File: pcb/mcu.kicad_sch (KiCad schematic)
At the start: 1 part, among them U1 STM32L432KCUx

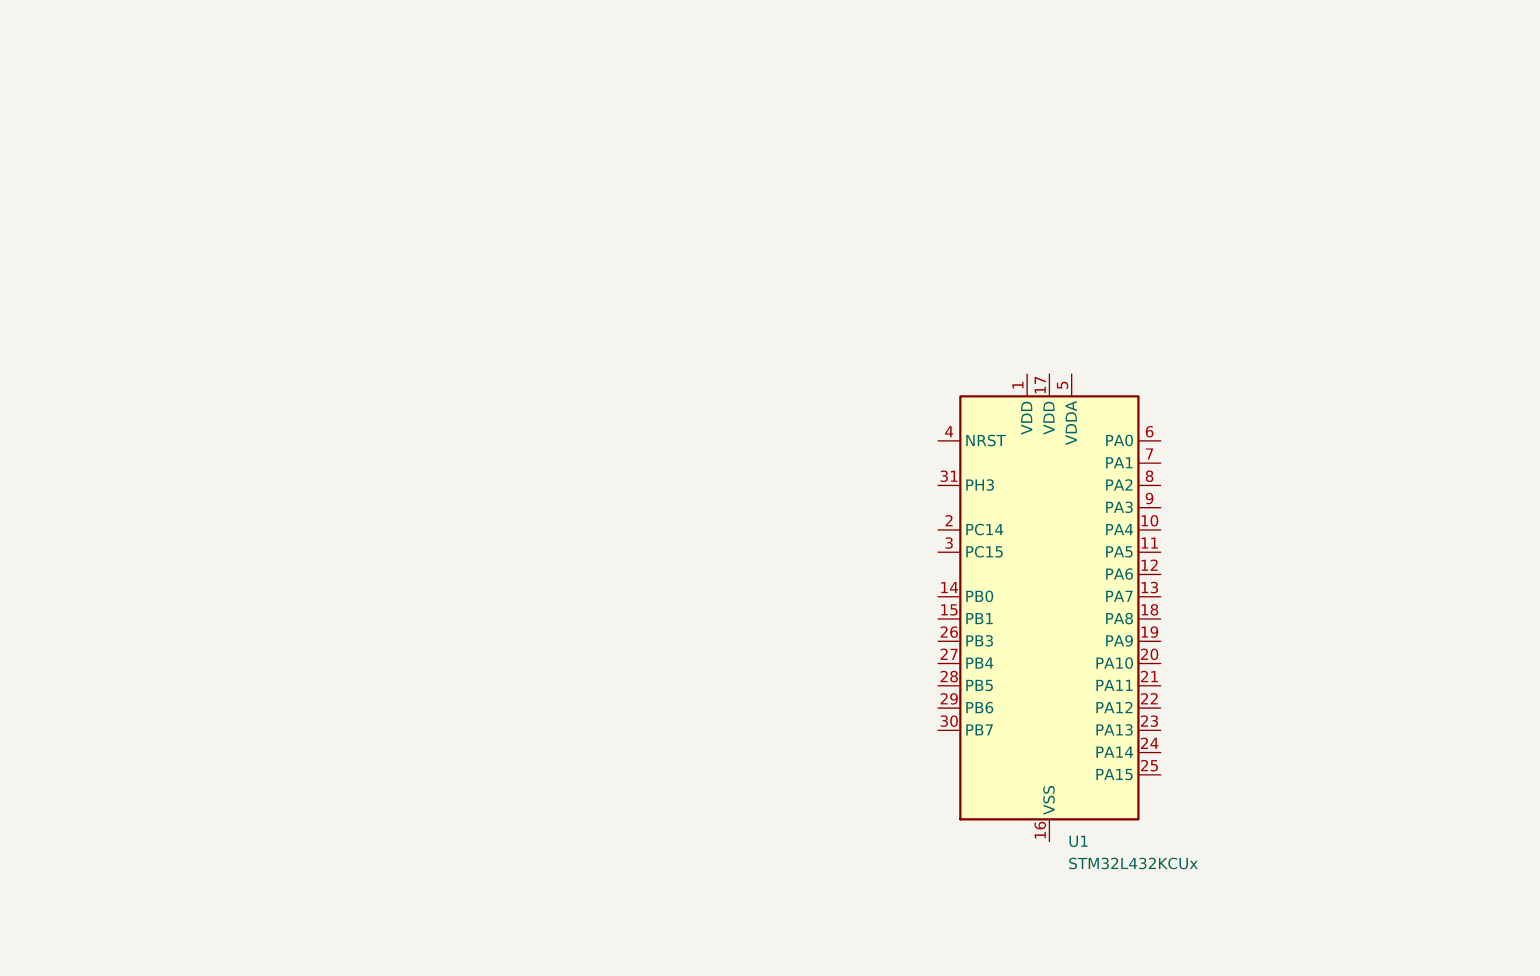
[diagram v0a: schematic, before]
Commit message: Sch almost done, maybe add current sense
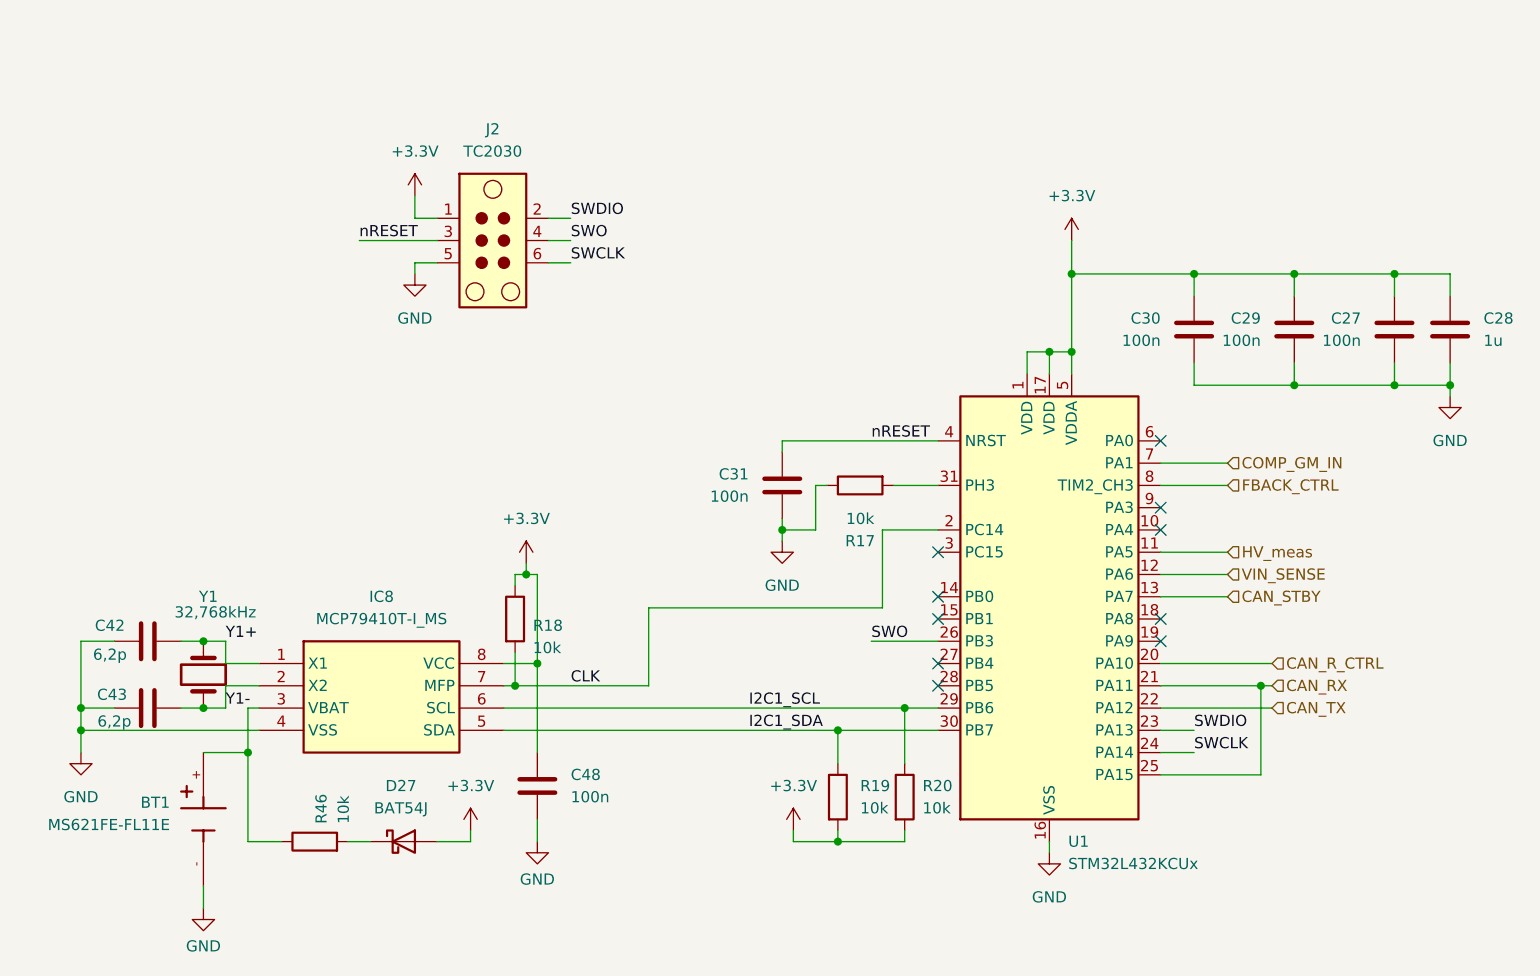
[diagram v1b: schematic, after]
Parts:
- added BT1: MS621FE-FL11E, Battery:BAT_MS621FE-FL11E, symbol MS621FE-FL11E:MS621FE-FL11E
- added C27, C29, C30, C31: 100n, Capacitor_SMD:C_0603_1608Metric, symbol Device:C
- added C28: 1u, Capacitor_SMD:C_0603_1608Metric, symbol Device:C
- added C42, C43: 6,2p, Capacitor_SMD:C_0402_1005Metric_Pad0.74x0.62mm_HandSolder, symbol Device:C
- added C48: 100n, Capacitor_SMD:C_0603_1608Metric_Pad1.08x0.95mm_HandSolder, symbol Device:C
- added D27: BAT54J, Diode_SMD:D_SOD-323F, symbol Diode:BAT54J
- added IC8: MCP79410T-I_MS, SOP65P490X110-8N, symbol SamacSys_Parts:MCP79410T-I_MS
- added J2: TC2030, Connector:Tag-Connect_TC2030-IDC-NL_2x03_P1.27mm_Vertical, symbol Connector:TC2030
- added R17: 10k, Resistor_SMD:R_0603_1608Metric, symbol Device:R
- added R18, R19, R20, R46: 10k, Resistor_SMD:R_0603_1608Metric_Pad0.98x0.95mm_HandSolder, symbol Device:R
- added Y1: 32,768kHz, Crystal:Crystal_SMD_MicroCrystal_CC7V-T1A-2Pin_3.2x1.5mm, symbol Device:Crystal
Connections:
- net +3.3V: now reaches U1.1 (VDD)
- net +3.3V: now also U1.17 (VDD), U1.5 (VDDA), C27.2, C28.1, C29.2, C30.2, C48.1, D27.2 (A), IC8.8 (VCC), J2.1, R18.1, R19.2, R20.2
- net HV_meas: now reaches U1.11 (PA5)
- net VIN_SENSE: now reaches U1.12 (PA6)
- net CAN_STBY: now reaches U1.13 (PA7)
- net GND: now reaches U1.16 (VSS), U1.32 (VSS), U1.33 (VSS)
- net GND: now also BT1.-, C27.1, C28.2, C29.1, C30.1, C31.1, C42.1, C43.1, C48.2, IC8.4 (VSS), J2.5, R17.1
- net CLK: now reaches U1.2 (PC14)
- net CLK: now also IC8.7 (MFP), R18.2
- net CAN_R_CTRL: now reaches U1.20 (PA10)
- net CAN_RX: now reaches U1.21 (PA11)
- net CAN_RX: now also U1.25 (PA15)
- net CAN_TX: now reaches U1.22 (PA12)
- net SWDIO: now reaches U1.23 (PA13)
- net SWDIO: now also J2.2
- net SWCLK: now reaches U1.24 (PA14)
- net SWCLK: now also J2.6
- net SWO: now reaches U1.26 (PB3)
- net SWO: now also J2.4
- net I2C1_SCL: now reaches U1.29 (PB6)
- net I2C1_SCL: now also IC8.6 (SCL), R20.1
- net I2C1_SDA: now reaches U1.30 (PB7)
- net I2C1_SDA: now also IC8.5 (SDA), R19.1
- net at U1.31 (PH3): now also R17.2
- net nRESET: now reaches U1.4 (NRST)
- net nRESET: now also C31.2, J2.3
- net COMP_GM_IN: now reaches U1.7 (PA1)
- net FBACK_CTRL: now reaches U1.8 (PA2)
- new net: BT1.+, IC8.3 (VBAT), R46.1
- new net: D27.1 (K), R46.2
- new net Y1+: C42.2, IC8.1 (X1), Y1.1
- new net Y1-: C43.2, IC8.2 (X2), Y1.2
- no-connect marks 0 -> 10

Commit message: Scheamtic almost finished, astarted firmware and pcb
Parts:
- added C38: 1u, Capacitor_SMD:C_0603_1608Metric, symbol Device:C
- added FB3: BLM31PG601SN1L, Inductor_SMD:L_1206_3216Metric, symbol Device:FerriteBead
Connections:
- net +3.3V: now also FB3.1; no longer C27.2, U1.5 (VDDA)
- net CAN_STBY: now also U1.19 (PA9); no longer U1.13 (PA7)
- net GND: now also C38.2
- net EN_I_SENS: now reaches U1.14 (PB0)
- net COMP_GM_IN renamed COMP_GM
- new net: C27.2, C38.1, FB3.2, U1.5 (VDDA)
- new net I_SENS: U1.13 (PA7)
- no-connect marks 10 -> 8
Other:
- moved on the sheet: C31

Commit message: Schematic finished, first routing
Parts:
- removed BT1: MS621FE-FL11E, Battery:BAT_MS621FE-FL11E, symbol MS621FE-FL11E:MS621FE-FL11E
- added BT1: MS621FE-FL11E, lib_local:BAT_MS621FE-FL11E, symbol Device:Battery_Cell
- IC8: footprint SOP65P490X110-8N -> SamacSys_Parts:SOP65P490X110-8N
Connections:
- net GND: now also BT1.2 (-)
- net at IC8.3 (VBAT), R46.1: now also BT1.1 (+)
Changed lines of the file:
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@@
 	(wire
 		(pts
+			(xy 52.07 116.84) (xy 52.07 121.92)
+		)
+		(stroke
+			(width 0)
+			(type default)
+		)
+	)
+	(wire
+		(pts
 			(xy 151.13 33.02) (xy 151.13 30.48)
 		)
@@
 	(wire
 		(pts
+			(xy 52.07 104.14) (xy 52.07 109.22)
+		)
+		(stroke
+			(width 0)
+			(type default)
+		)
+	)
+	(wire
+		(pts
 			(xy 130.81 73.66) (xy 135.89 73.66)
 		)
@@
 	(wire
 		(pts
-			(xy 52.07 119.38) (xy 52.07 121.92)
-		)
-		(stroke
-			(width 0)
-			(type default)
-		)
-	)
-	(wire
-		(pts
 			(xy 68.58 114.3) (xy 71.12 114.3)
 		)
@@
 	)
 	(symbol
-		(lib_id "MS621FE-FL11E:MS621FE-FL11E")
-		(at 52.07 111.76 90)
-		(mirror x)
-		(unit 1)
-		(body_style 1)
-		(exclude_from_sim no)
-		(in_bom yes)
-		(on_board yes)
-		(in_pos_files yes)
-		(dnp no)
-		(property "Reference" "BT1"
-			(at 48.26 109.8549 90)
-			(show_name no)
-			(do_not_autoplace no)
-			(effects
-				(font
-					(size 1.27 1.27)
-				)
-				(justify left)
-			)
-		)
-		(property "Value" "MS621FE-FL11E"
-			(at 48.26 112.3949 90)
-			(show_name no)
-			(do_not_autoplace no)
-			(effects
-				(font
-					(size 1.27 1.27)
-				)
-				(justify left)
-			)
-		)
-		(property "Footprint" "Battery:BAT_MS621FE-FL11E"
-			(at 52.07 111.76 0)
-			(hide yes)
-			(show_name no)
-			(do_not_autoplace no)
-			(effects
-				(font
-					(size 1.27 1.27)
-				)
-				(justify bottom)
-			)
-		)
-		(property "Datasheet" ""
-			(at 52.07 111.76 0)
-			(hide yes)
-			(show_name no)
-			(do_not_autoplace no)
-			(effects
-				(font
-					(size 1.27 1.27)
-				)
-			)
-		)
-		(property "Description" ""
-			(at 52.07 111.76 0)
-			(hide yes)
-			(show_name no)
-			(do_not_autoplace no)
-			(effects
-				(font
-					(size 1.27 1.27)
-				)
-			)
-		)
-		(property "MF" "Seiko Instruments"
-			(at 52.07 111.76 0)
-			(hide yes)
-			(show_name no)
-			(do_not_autoplace no)
-			(effects
-				(font
-					(size 1.27 1.27)
-				)
-				(justify bottom)
-			)
-		)
-		(property "MAXIMUM_PACKAGE_HEIGHT" "2.8mm"
-			(at 52.07 111.76 0)
-			(hide yes)
-			(show_name no)
-			(do_not_autoplace no)
-			(effects
-				(font
-					(size 1.27 1.27)
-				)
-				(justify bottom)
-			)
-		)
-		(property "Package" "QFP-128 Seiko"
-			(at 52.07 111.76 0)
-			(hide yes)
-			(show_name no)
-			(do_not_autoplace no)
-			(effects
-				(font
-					(size 1.27 1.27)
-				)
-				(justify bottom)
-			)
-		)
-		(property "Price" "None"
-			(at 52.07 111.76 0)
-			(hide yes)
-			(show_name no)
-			(do_not_autoplace no)
-			(effects
-				(font
-					(size 1.27 1.27)
-				)
-				(justify bottom)
-			)
-		)
-		(property "Check_prices" "https://www.snapeda.com/parts/MS621FE-FL11E/Seiko/view-part/?ref=eda"
-			(at 52.07 111.76 0)
-			(hide yes)
-			(show_name no)
-			(do_not_autoplace no)
-			(effects
-				(font
-					(size 1.27 1.27)
-				)
-				(justify bottom)
-			)
-		)
-		(property "STANDARD" "Manufacturer Recommendations"
-			(at 52.07 111.76 0)
-			(hide yes)
-			(show_name no)
-			(do_not_autoplace no)
-			(effects
-				(font
-					(size 1.27 1.27)
-				)
-				(justify bottom)
-			)
-		)
-		(property "PARTREV" "E"
-			(at 52.07 111.76 0)
-			(hide yes)
-			(show_name no)
-			(do_not_autoplace no)
-			(effects
-				(font
-					(size 1.27 1.27)
-				)
-				(justify bottom)
-			)
-		)
-		(property "SnapEDA_Link" "https://www.snapeda.com/parts/MS621FE-FL11E/Seiko/view-part/?ref=snap"
-			(at 52.07 111.76 0)
-			(hide yes)
-			(show_name no)
-			(do_not_autoplace no)
-			(effects
-				(font
-					(size 1.27 1.27)
-				)
-				(justify bottom)
-			)
-		)
-		(property "MP" "MS621FE-FL11E"
-			(at 52.07 111.76 0)
-			(hide yes)
-			(show_name no)
-			(do_not_autoplace no)
-			(effects
-				(font
-					(size 1.27 1.27)
-				)
-				(justify bottom)
-			)
-		)
-		(property "Description_1" "Coin, 6.8mm 3 V Lithium Battery Rechargeable (Secondary) 5.5mAh"
-			(at 52.07 111.76 0)
-			(hide yes)
-			(show_name no)
-			(do_not_autoplace no)
-			(effects
-				(font
-					(size 1.27 1.27)
-				)
-				(justify bottom)
-			)
-		)
-		(property "Availability" "In Stock"
-			(at 52.07 111.76 0)
-			(hide yes)
-			(show_name no)
-			(do_not_autoplace no)
-			(effects
-				(font
-					(size 1.27 1.27)
-				)
-				(justify bottom)
-			)
-		)
-		(property "MANUFACTURER" "Seiko Instruments"
-			(at 52.07 111.76 0)
-			(hide yes)
-			(show_name no)
-			(do_not_autoplace no)
-			(effects
-				(font
-					(size 1.27 1.27)
-				)
-				(justify bottom)
-			)
-		)
-		(pin "+"
-		)
-		(pin "-"
-		)
-		(instances
-			(project "geiger_probe"
-				(path "/eb6e66b6-2df0-4872-8f92-4c510b34f8fe/58ca81b1-4ff8-49ea-a8fc-6cd2a9c20a6b"
-					(reference "BT1")
-					(unit 1)
-				)
-			)
-		)
-	)
-	(symbol
 		(lib_id "Diode:BAT54J")
 		(at 74.93 114.3 0)
@@
 			)
 		)
-		(property "Footprint" "SOP65P490X110-8N"
+		(property "Footprint" "SamacSys_Parts:SOP65P490X110-8N"
 			(at 82.55 188.9 0)
 			(hide yes)
@@
 					(unit 1)
 				)
+			)
+		)
+	)
+	(symbol
+		(lib_id "Device:Battery_Cell")
+		(at 52.07 114.3 0)
+		(mirror y)
+		(unit 1)
+		(body_style 1)
+		(exclude_from_sim no)
+		(in_bom yes)
+		(on_board yes)
+		(in_pos_files yes)
+		(dnp no)
+		(property "Reference" "BT1"
+			(at 48.26 111.1884 0)
+			(show_name no)
+			(do_not_autoplace no)
+			(effects
+				(font
+					(size 1.27 1.27)
+				)
+				(justify left)
+			)
+		)
+		(property "Value" "MS621FE-FL11E"
+			(at 48.26 113.7284 0)
+			(show_name no)
+			(do_not_autoplace no)
+			(effects
+				(font
+					(size 1.27 1.27)
+				)
+				(justify left)
+			)
+		)
+		(property "Footprint" "lib_local:BAT_MS621FE-FL11E"
+			(at 52.07 112.776 90)
+			(hide yes)
+			(show_name no)
+			(do_not_autoplace no)
+			(effects
+				(font
+					(size 1.27 1.27)
+				)
+			)
+		)
+		(property "Datasheet" ""
+			(at 52.07 112.776 90)
+			(hide yes)
+			(show_name no)
+			(do_not_autoplace no)
+			(effects
+				(font
+					(size 1.27 1.27)
+				)
+			)
+		)
+		(property "Description" "MS621FE-FL11E"
+			(at 52.07 114.3 0)
+			(hide yes)
+			(show_name no)
+			(do_not_autoplace no)
+			(effects
+				(font
+					(size 1.27 1.27)
+				)
+			)
+		)
+		(property "Sim.Device" "V"
+			(at 52.07 114.3 0)
+			(hide yes)
+			(show_name no)
+			(do_not_autoplace no)
+			(effects
+				(font
+					(size 1.27 1.27)
+				)
+			)
+		)
+		(property "Sim.Type" "DC"
+			(at 52.07 114.3 0)
+			(hide yes)
+			(show_name no)
+			(do_not_autoplace no)
+			(effects
+				(font
+					(size 1.27 1.27)
+				)
+			)
+		)
+		(property "Sim.Pins" "1=+ 2=-"
+			(at 52.07 114.3 0)
+			(hide yes)
+			(show_name no)
+			(do_not_autoplace no)
+			(effects
+				(font
+					(size 1.27 1.27)
+				)
+			)
+		)
+		(pin "2"
+		)
+		(pin "1"
+		)
+		(instances
+			(project "geiger_probe"
+				(path "/eb6e66b6-2df0-4872-8f92-4c510b34f8fe/58ca81b1-4ff8-49ea-a8fc-6cd2a9c20a6b"
+					(reference "BT1")
+					(unit 1)
+				)
